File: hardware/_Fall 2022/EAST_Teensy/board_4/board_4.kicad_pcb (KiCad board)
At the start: 2 copper layers, 10 parts, among them J1 Conn_01x04, J2 Conn_02x10_Counter_Clockwise, U1 Teensy4.1

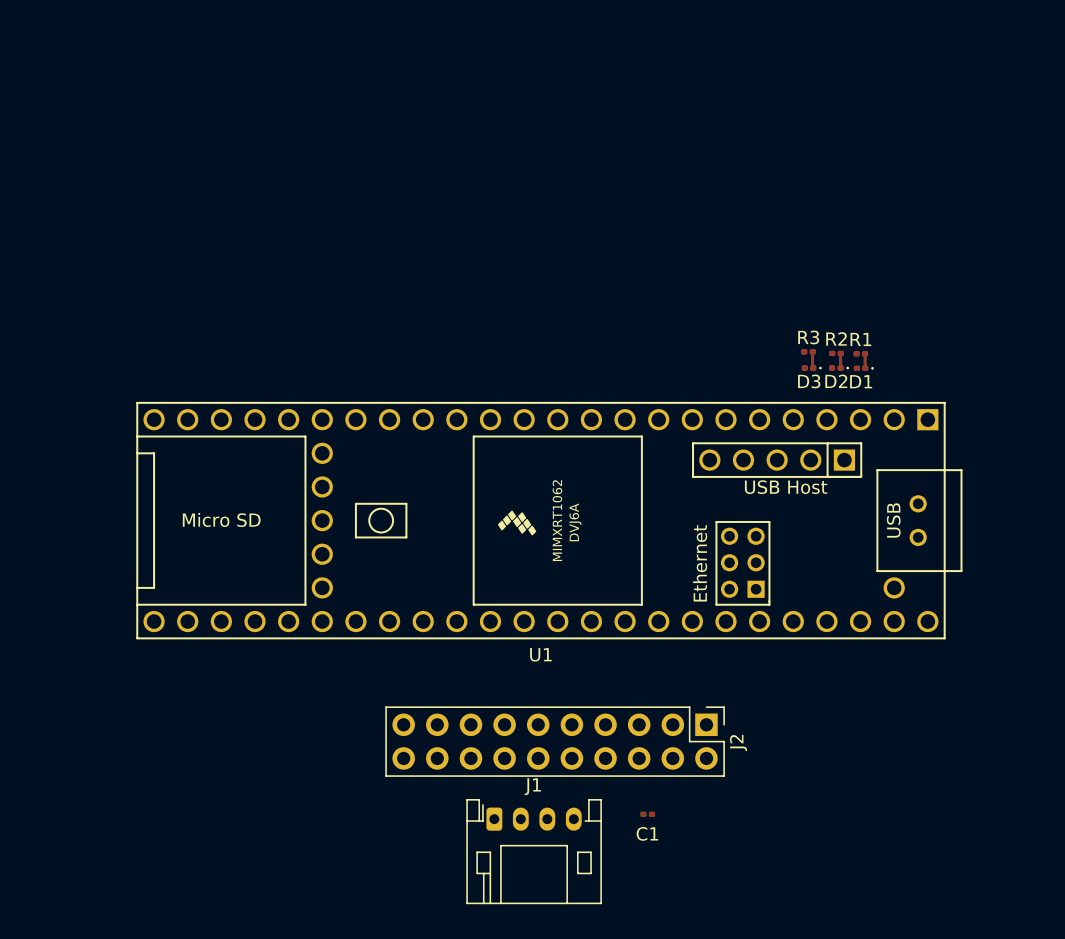
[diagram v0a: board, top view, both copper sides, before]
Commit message: Update pin connections
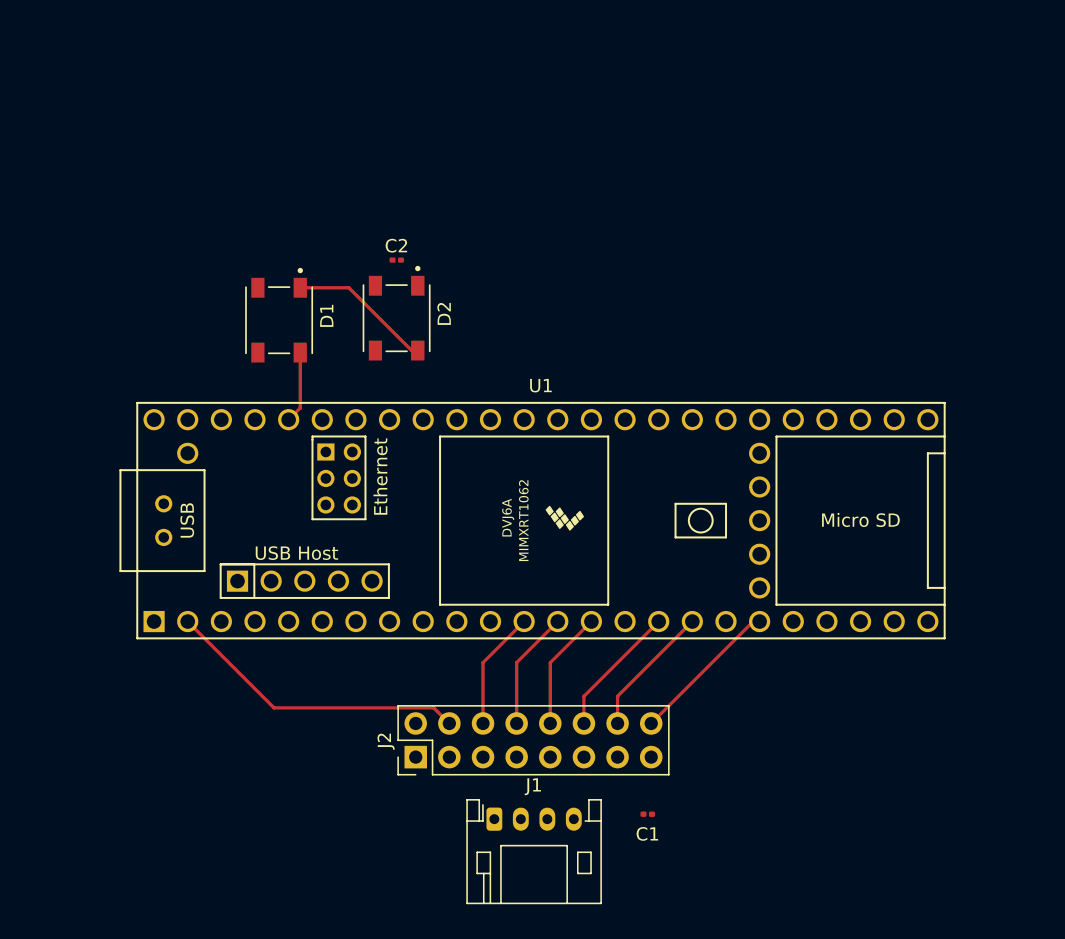
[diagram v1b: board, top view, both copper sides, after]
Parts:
- removed D3: LED, LED_SMD:LED_0201_0603Metric
- removed R1, R2, R3: 150, Resistor_SMD:R_0201_0603Metric
- added C2: 0.1uf, Capacitor_SMD:C_0201_0603Metric, F.Cu at (137.7, 102.9)
- D1: value LED -> Neopixel1; footprint LED_SMD:LED_0201_0603Metric -> Neopixel:LED_1655
- D2: value LED -> Neopixel2; footprint LED_SMD:LED_0201_0603Metric -> Neopixel:LED_1655
- J2: value Conn_02x10_Counter_Clockwise -> Conn_02x08_Odd_Even; footprint Connector_PinHeader_2.54mm:PinHeader_2x10_P2.54mm_Vertical -> Connector_PinHeader_2.54mm:PinHeader_2x08_P2.54mm_Vertical
- moved D1 44.1 mm to (128.8, 107.5), turned to -90 degrees
- moved D2 33.4 mm to (137.7, 107.3), turned to -90 degrees
- moved J2 22.1 mm to (139.2, 140.5), turned to 90 degrees
- turned U1 to 0 degrees
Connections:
- D1 pad 2: /LED 0 -> GND
- D2 pad 1: Net-(D2-Pad1) -> unconnected-(D2-Pad1)
- D2 pad 2: /LED 1 -> GND
- J2 pad 1: GND -> /RX 2
- J2 pad 10: /CS 5 -> /MISO 1
- J2 pad 11: /TX 3 -> /TX 1
- J2 pad 12: /RX 3 -> /SCL 2
- J2 pad 13: /TX 2 -> /RX 1
- J2 pad 14: /RX 2 -> /SDA 2
- J2 pad 15: /TX 1 -> /CS 3
- J2 pad 16: /RX 1 -> /SCK 1
- J2 pad 2: /3.3V -> GND
- J2 pad 3: /MOSI 1 -> /TX 2
- J2 pad 4: /MISO 1 -> /CS 1
- J2 pad 5: /SCK 1 -> /SCL 1
- J2 pad 6: /CS 1 -> /CS 2
- J2 pad 7: /CS 2 -> /SDA 1
- J2 pad 8: /CS 3 -> /MOSI 1
- J2 pad 9: /CS 4 -> /3.3V
- U1 pad 13: unconnected-(U1-Pad13) -> /MOSI 1
- U1 pad 14: unconnected-(U1-Pad14) -> /MISO 1
- U1 pad 18: /MOSI 1 -> unconnected-(U1-Pad18)
- U1 pad 26: /TX 3 -> /TX 0
- U1 pad 27: /RX 3 -> /RX 0
- U1 pad 28: /CS 4 -> unconnected-(U1-Pad28)
- U1 pad 30: /CS 5 -> unconnected-(U1-Pad30)
- U1 pad 31: /MISO 1 -> unconnected-(U1-Pad31)
- U1 pad 36: /TX 2 -> unconnected-(U1-Pad36)
- U1 pad 37: /RX 2 -> unconnected-(U1-Pad37)
- U1 pad 38: /TX 1 -> /RX 1
- U1 pad 39: /RX 1 -> /TX 1
- U1 pad 4: /LED 0 -> unconnected-(U1-Pad4)
- U1 pad 42: /TX 0 -> /RX 2
- U1 pad 43: /RX 0 -> /TX 2
- U1 pad 44: unconnected-(U1-Pad44) -> /NEOPIXEL
- U1 pad 5: /LED 1 -> unconnected-(U1-Pad5)
- U1 pad 6: /LED 2 -> unconnected-(U1-Pad6)
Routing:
- net /CS 1: track 0.00 -> 22.9 mm
- net /SCK 1: track 0.00 -> 11.4 mm
- net /SDA 2: track 0.00 -> 10.0 mm
- net /SCL 2: track 0.00 -> 10.0 mm
- net Net-(D1-Pad1): track 1.10 -> 10.8 mm
- net /MISO 1: track 0.00 -> 8.98 mm
- net /MOSI 1: track 0.00 -> 8.98 mm
- net /CS 2: track 0.00 -> 8.98 mm
- net /NEOPIXEL: track 0.00 -> 5.42 mm
- net Net-(D3-Pad1): track 1.24 -> 0.00 mm
- net Net-(D2-Pad1): track 1.11 -> 0.00 mm

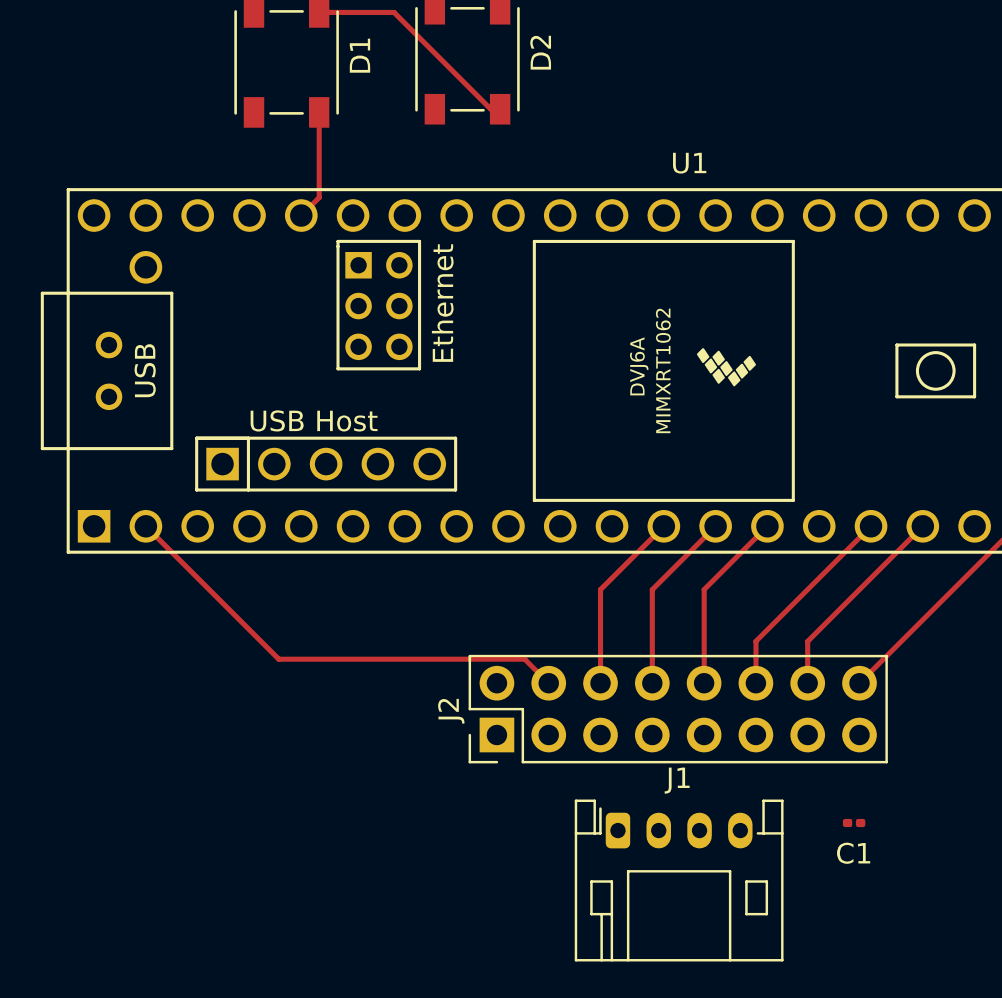
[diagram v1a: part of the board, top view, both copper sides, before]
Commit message: Complete PRISM Teensy layout
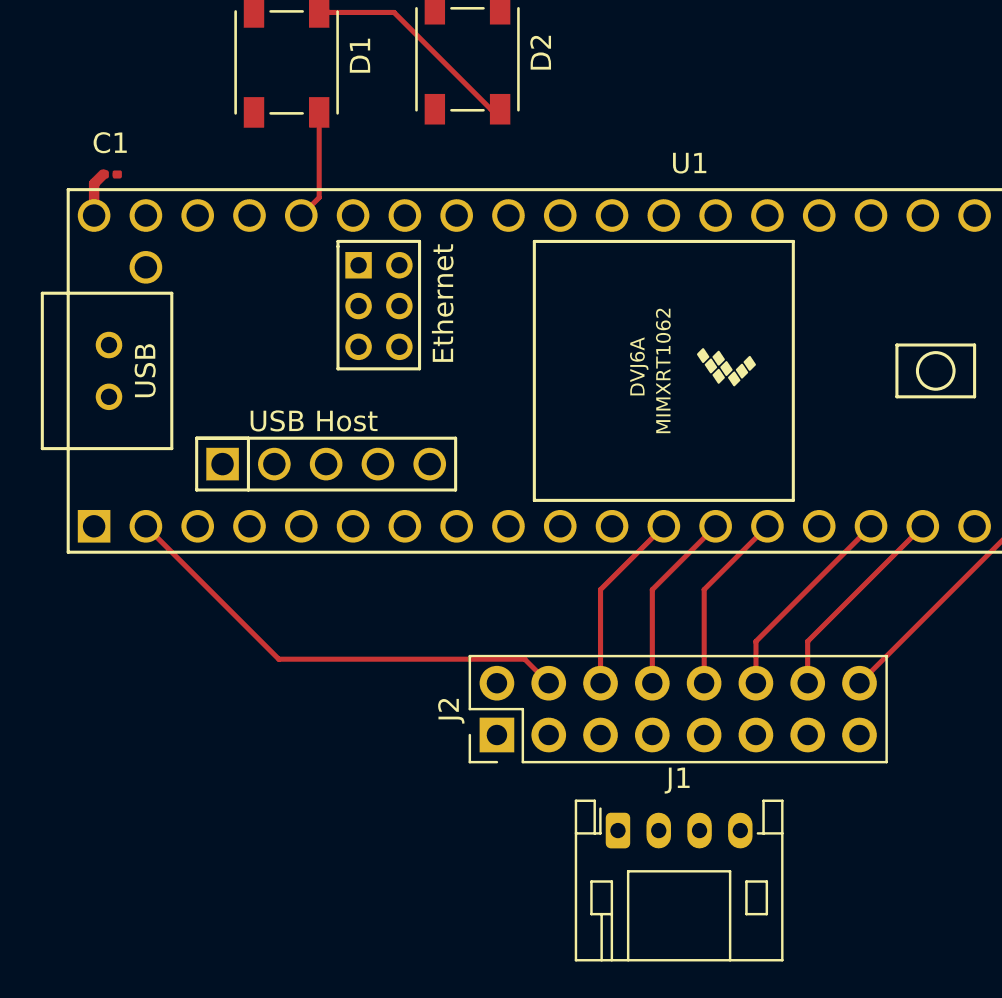
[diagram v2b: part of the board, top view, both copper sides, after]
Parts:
- moved C1 48.4 mm to (120.2, 113.0), turned to 0 degrees
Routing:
- net /V_BATT: track 0.00 -> 2.20 mm
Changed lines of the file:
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@@
   )
   (footprint "Capacitor_SMD:C_0201_0603Metric" (layer "F.Cu")
-    (at 156.68 144.78 180)
+    (at 120.225 112.975)
     (descr "Capacitor SMD 0201 (0603 Metric), square (rectangular) end terminal, IPC_7351 nominal, (Body size source: https://www.vishay.com/docs/20052/crcw0201e3.pdf), generated with kicad-footprint-generator")
     (tags "capacitor")
@@
     (fp_line (start -0.3 -0.15) (end 0.3 -0.15) (layer "F.Fab") (width 0.1))
     (fp_line (start -0.3 0.15) (end -0.3 -0.15) (layer "F.Fab") (width 0.1))
-    (pad "" smd roundrect (at -0.345 0 180) (size 0.318 0.36) (layers "F.Paste") (roundrect_rratio 0.25))
-    (pad "" smd roundrect (at 0.345 0 180) (size 0.318 0.36) (layers "F.Paste") (roundrect_rratio 0.25))
-    (pad "1" smd roundrect (at -0.32 0 180) (size 0.46 0.4) (layers "F.Cu" "F.Mask") (roundrect_rratio 0.25)
+    (pad "" smd roundrect (at -0.345 0) (size 0.318 0.36) (layers "F.Paste") (roundrect_rratio 0.25))
+    (pad "" smd roundrect (at 0.345 0) (size 0.318 0.36) (layers "F.Paste") (roundrect_rratio 0.25))
+    (pad "1" smd roundrect (at -0.32 0) (size 0.46 0.4) (layers "F.Cu" "F.Mask") (roundrect_rratio 0.25)
       (net 1 "/V_BATT") (pintype "passive"))
-    (pad "2" smd roundrect (at 0.32 0 180) (size 0.46 0.4) (layers "F.Cu" "F.Mask") (roundrect_rratio 0.25)
+    (pad "2" smd roundrect (at 0.32 0) (size 0.46 0.4) (layers "F.Cu" "F.Mask") (roundrect_rratio 0.25)
       (net 2 "GND") (pintype "passive"))
     (model "${KICAD6_3DMODEL_DIR}/Capacitor_SMD.3dshapes/C_0201_0603Metric.wrl"
@@
   (gr_line (start 122.698438 153) (end 173.1 153) (layer "Dwgs.User") (width 0.2))
   (gr_circle (center 175.394719 140.299534) (end 173.565919 140.299534) (layer "Dwgs.User") (width 0.2) (fill none))
+  (segment (start 119.41 113.426) (end 119.861 112.975) (width 0.508) (layer "F.Cu") (net 1))
+  (segment (start 119.41 114.99) (end 119.41 113.426) (width 0.508) (layer "F.Cu") (net 1))
   (segment (start 130.45 105.03) (end 134.12 105.03) (width 0.25) (layer "F.Cu") (net 3))
   (segment (start 134.12 105.03) (end 138.8675 109.7775) (width 0.25) (layer "F.Cu") (net 3))

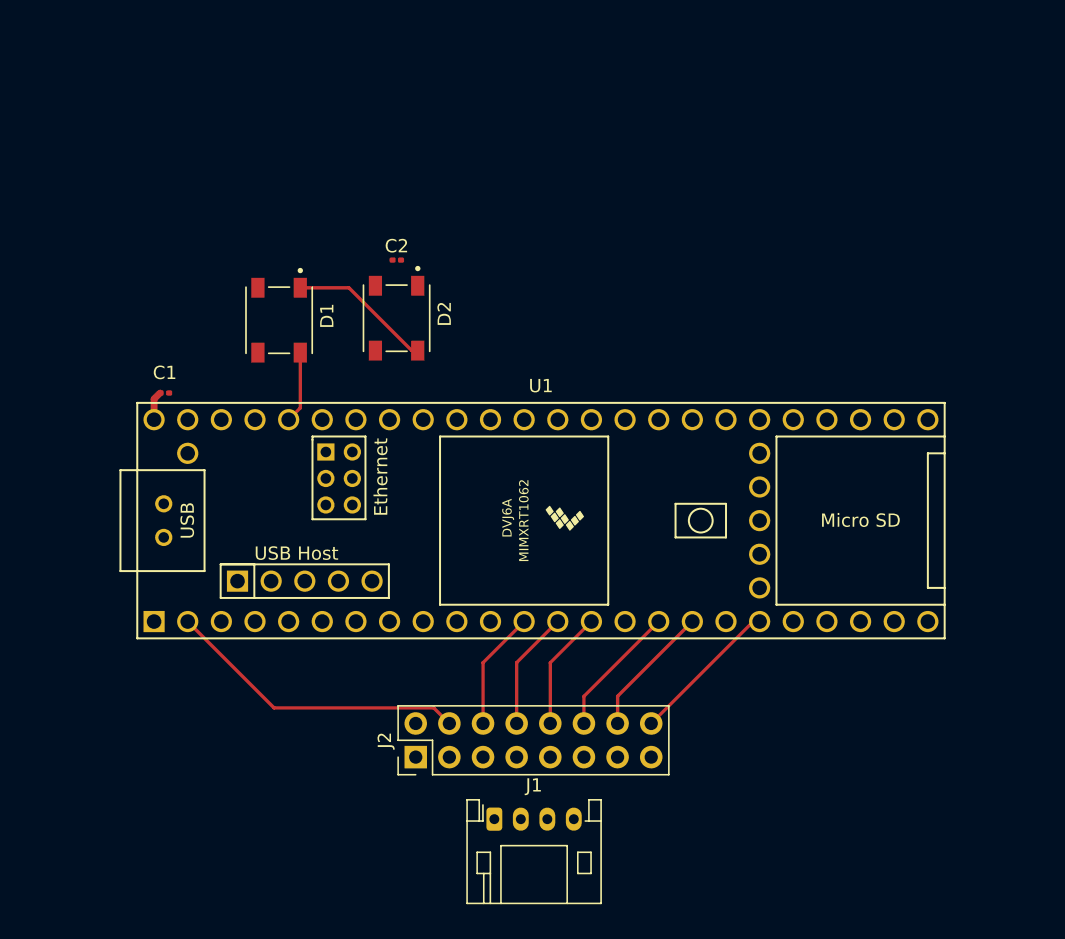
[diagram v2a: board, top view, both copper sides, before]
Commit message: Completed EAST Teensy board, confused at GPS board
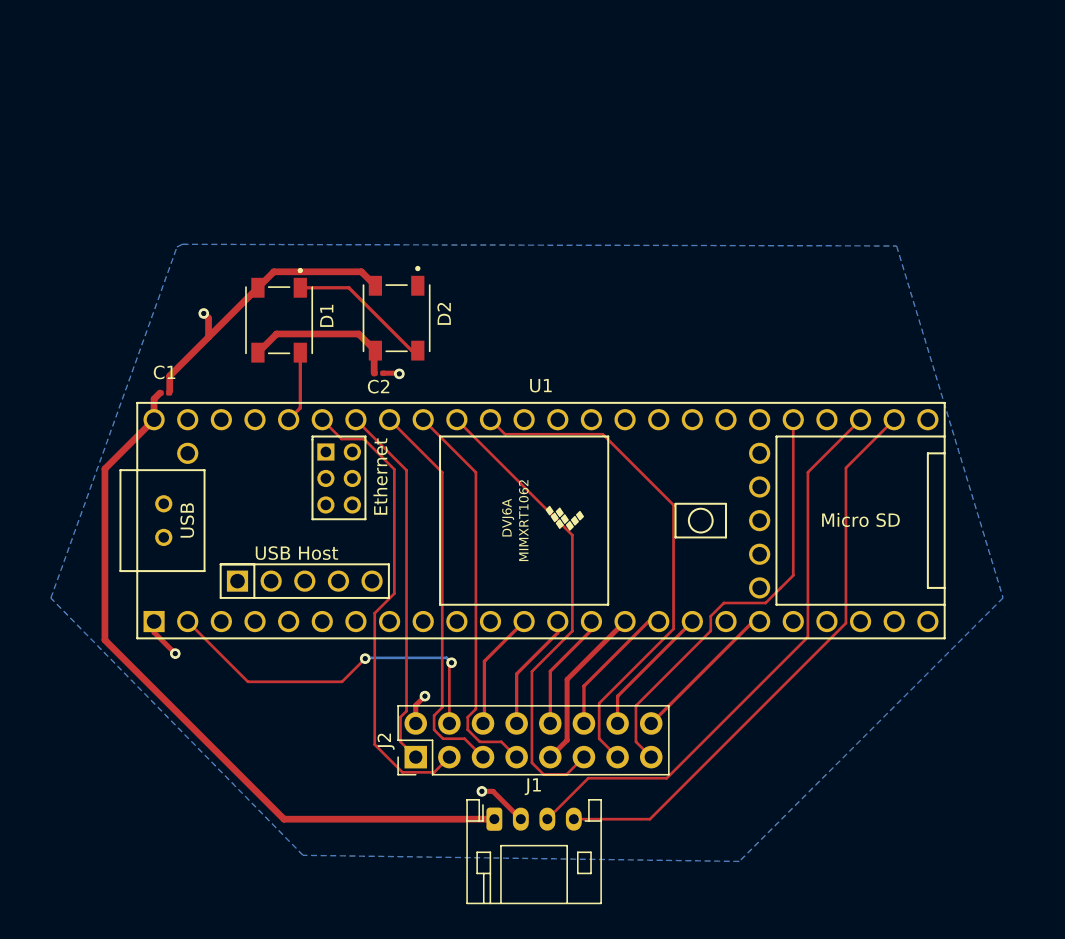
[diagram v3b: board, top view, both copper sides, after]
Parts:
- moved C2 8.65 mm to (136.4, 111.5), turned to 180 degrees
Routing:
- net /V_BATT: track 2.20 -> 55.4 mm
- net /TX 0: track 0.00 -> 43.5 mm
- net /RX 0: track 0.00 -> 43.4 mm
- net /RX 1: track 0.00 -> 38.4 mm
- net /TX 1: track 0.00 -> 35.6 mm
- net /TX 2: track 0.00 -> 35.4 mm
- net GND: track 0.00 -> 32.8 mm, vias 0 -> 5
- net /CS 3: track 0.00 -> 32.7 mm
- net /SDA 1: track 0.00 -> 29.9 mm
- net /SCL 1: track 0.00 -> 29.9 mm
- net /RX 2: track 0.00 -> 27.7 mm
- net /3.3V: track 0.00 -> 12.6 mm
- net +3.3V: track 0.00 -> 11.7 mm
- net /CS 1: track 22.9 -> 27.4 mm, vias 0 -> 2
- added copper zone on B.Cu, net GND
